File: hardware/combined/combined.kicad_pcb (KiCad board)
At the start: 2 copper layers, 62 x 208.5 mm, 151 parts, among them J1 USB-C 5V in, J2 Mini-DIN-8 to printer, J4 Mini-DIN-8 LocalTalk, SW1 EVQP44B3M, SW2 B3U-1000P, SW3 TS-1002-BR15026, U1 ESP32-S3-WROOM-1-N8R2, U2 SP3490EN-L, U3 SP3232EBEN-L/TR, U4 AP7361C-33E, U5 USBLC6-2SC6, U6 SP3485EN-L, U7 PIC12F1840-I/P, U8 SP3485EN-L, U9 SN74LV1T125DCKR

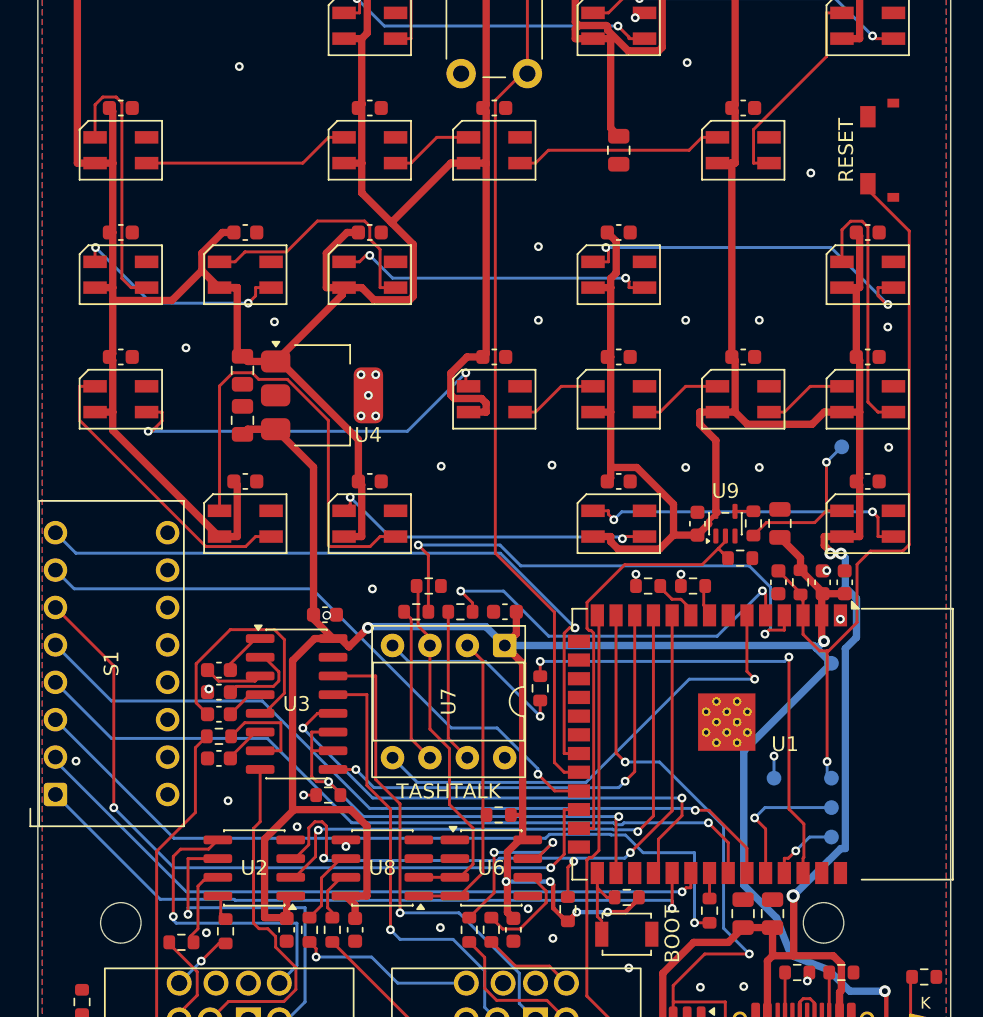
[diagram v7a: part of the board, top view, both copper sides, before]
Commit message: Rev 2026.11: no DIP switches, own handshake pins, the Macintosh Mini's reset switch (W-1091)
Wells dropped the DIP switches: the settings page already does what they
did. With S1 and R28 gone, the freed pins give each port's HSKo its own
GPIO (J2 on IO47 with R24, J4 on IO13) and J4's HSKi moves to IO21, so
IO35-IO37 are free and the board takes an octal-PSRAM module as well as a
quad one. J4's drive has no pull-down: one would sit at the end of an 8 mm
stub, and nothing on J4 reads pin 1 at power-up.

SW1 becomes the BZCN TSB001A3518A, the Macintosh Mini's side switch, held
by two pegs and two bracket pads where the EVQP44B3M lifted off its pads.
Its footprint and model are drawn here (r13_mkfp_sw1.py, make_sw1_model.py);
its RESET label is board silk now. r13_build.sh stops at a failed step.

Refs: W-1091
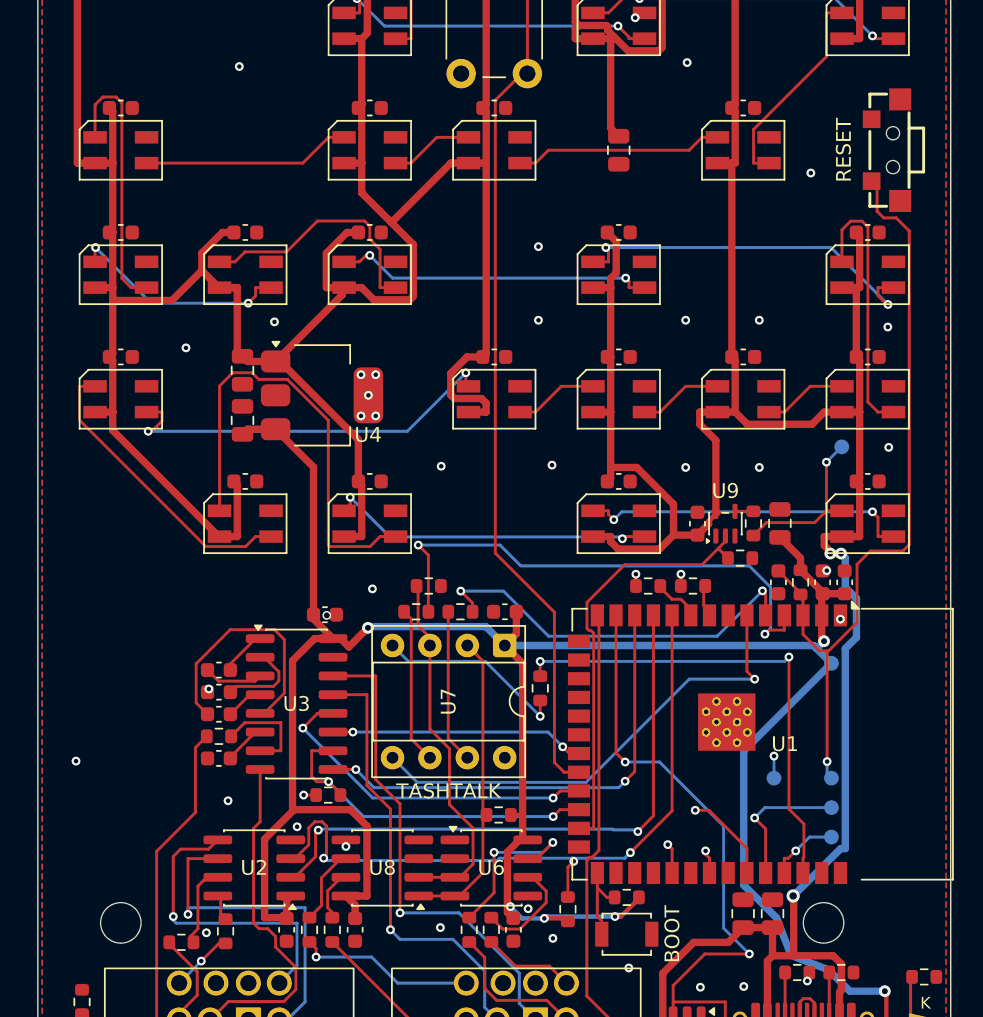
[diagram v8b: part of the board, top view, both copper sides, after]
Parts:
- removed R28: 1k, Resistor_SMD:R_0603_1608Metric
- removed S1: DIP switch, 8-position, airwriter:SW_DIP_8_RightAngle_DP-08RP
- SW1: value EVQP44B3M -> TSB001A3518A; footprint airwriter:EVQP44B3M_SidePress -> airwriter:SW_BZCN_TSB001A3518A
- moved SW1 0.38 mm to (157.6, 99.5), turned to -90 degrees
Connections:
- U1 pad 21: /DIP8 -> /J4_HSKO_DRV
- U1 pad 23: /DIP7 -> /J4_HSKI_RX
- U1 pad 24: /DIP6 -> /HSKI_DRV
- U1 pad 28: /HSKI_DRV -> unconnected-(U1-IO35-Pad28)
- U1 pad 30: /J4_HSKI_RX -> unconnected-(U1-IO37-Pad30)
- U1 pad 31: /DIP1 -> unconnected-(U1-IO38-Pad31)
- U1 pad 32: /DIP2 -> unconnected-(U1-IO39-Pad32)
- U1 pad 33: /DIP3_GPIO -> unconnected-(U1-IO40-Pad33)
- U1 pad 34: /DIP4 -> unconnected-(U1-IO41-Pad34)
- U1 pad 35: /DIP5 -> unconnected-(U1-IO42-Pad35)
- U3 pad 11: /HSKI_DRV -> /J4_HSKO_DRV
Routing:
- net /DIP5: track 54.4 -> 0.00 mm, vias 1 -> 0
- net /DIP3: track 53.1 -> 0.00 mm, vias 1 -> 0
- net /DIP4: track 52.4 -> 0.00 mm, vias 1 -> 0
- net /DIP6: track 51.9 -> 0.00 mm, vias 2 -> 0
- net /DIP2: track 48.2 -> 0.00 mm, vias 1 -> 0
- net /DIP8: track 48.0 -> 0.00 mm, vias 1 -> 0
- net /DIP1: track 47.8 -> 0.00 mm, vias 1 -> 0
- net /DIP7: track 42.0 -> 0.00 mm, vias 1 -> 0
- net /J4_HSKO_DRV: track 0.00 -> 17.3 mm, vias 0 -> 2
- net /J4_HSKI_RX: track 35.4 -> 23.4 mm
- net /HSKI_DRV: track 32.5 -> 23.3 mm
- net unconnected-(U1-IO42-Pad35): track 0.00 -> 6.44 mm, vias 0 -> 1
- net unconnected-(U1-IO38-Pad31): track 0.00 -> 2.25 mm, vias 0 -> 1
- net unconnected-(U1-IO40-Pad33): track 0.00 -> 1.79 mm, vias 0 -> 1
- net /DIP3_GPIO: track 1.68 -> 0.00 mm
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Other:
- board text added: "RESET"
